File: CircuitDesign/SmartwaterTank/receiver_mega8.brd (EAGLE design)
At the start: 100 x 80 mm, 13 parts, among them IC1 MEGA8-P, T1 2N2222

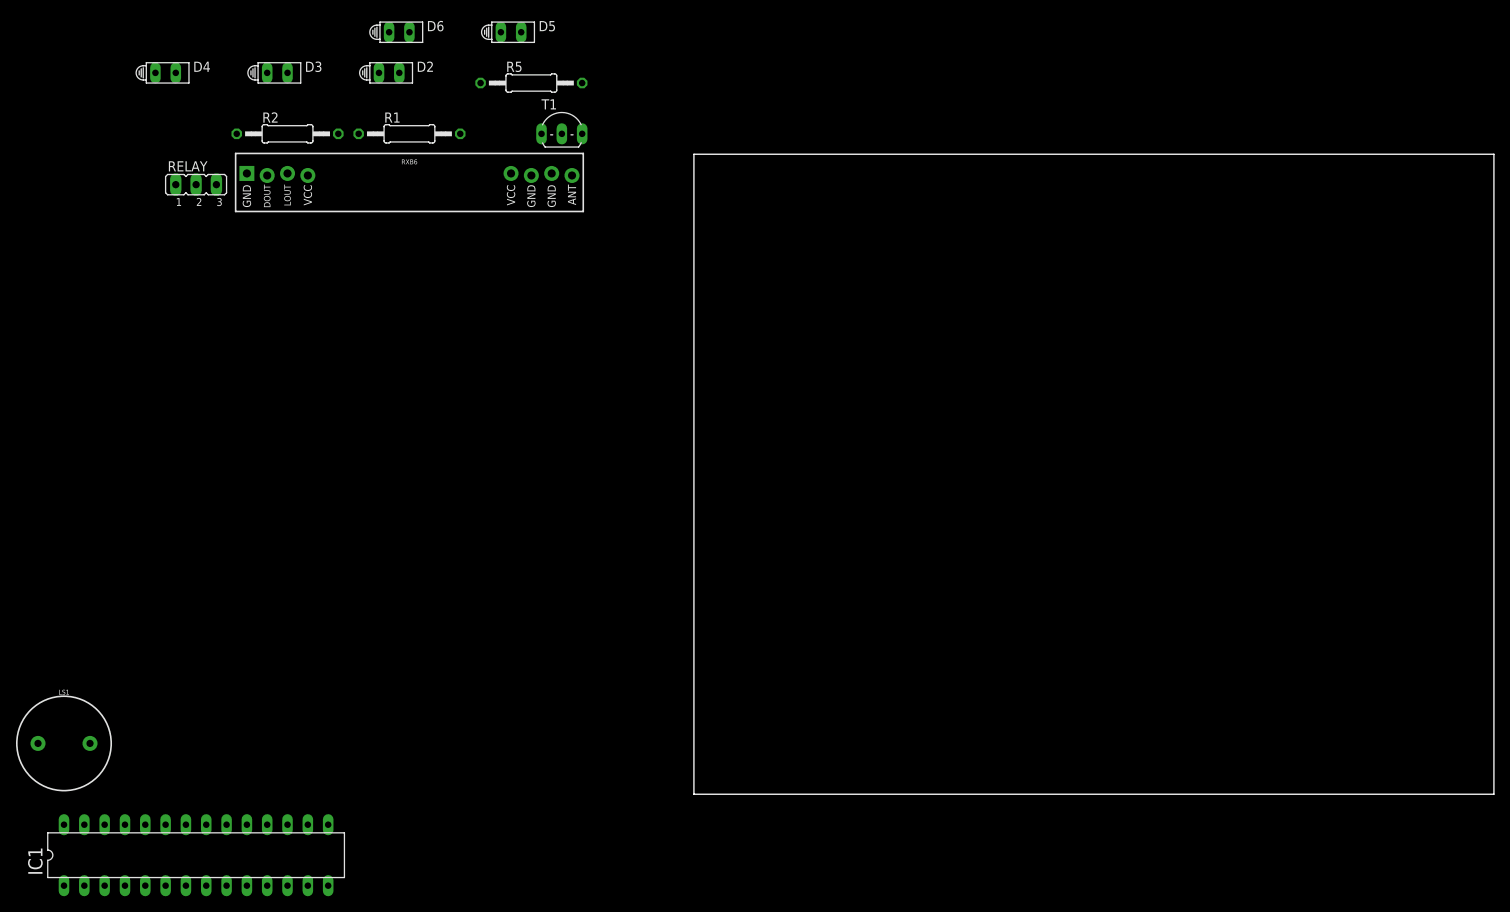
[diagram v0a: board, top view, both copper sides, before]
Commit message: Issue #6: update receiver board for vero board
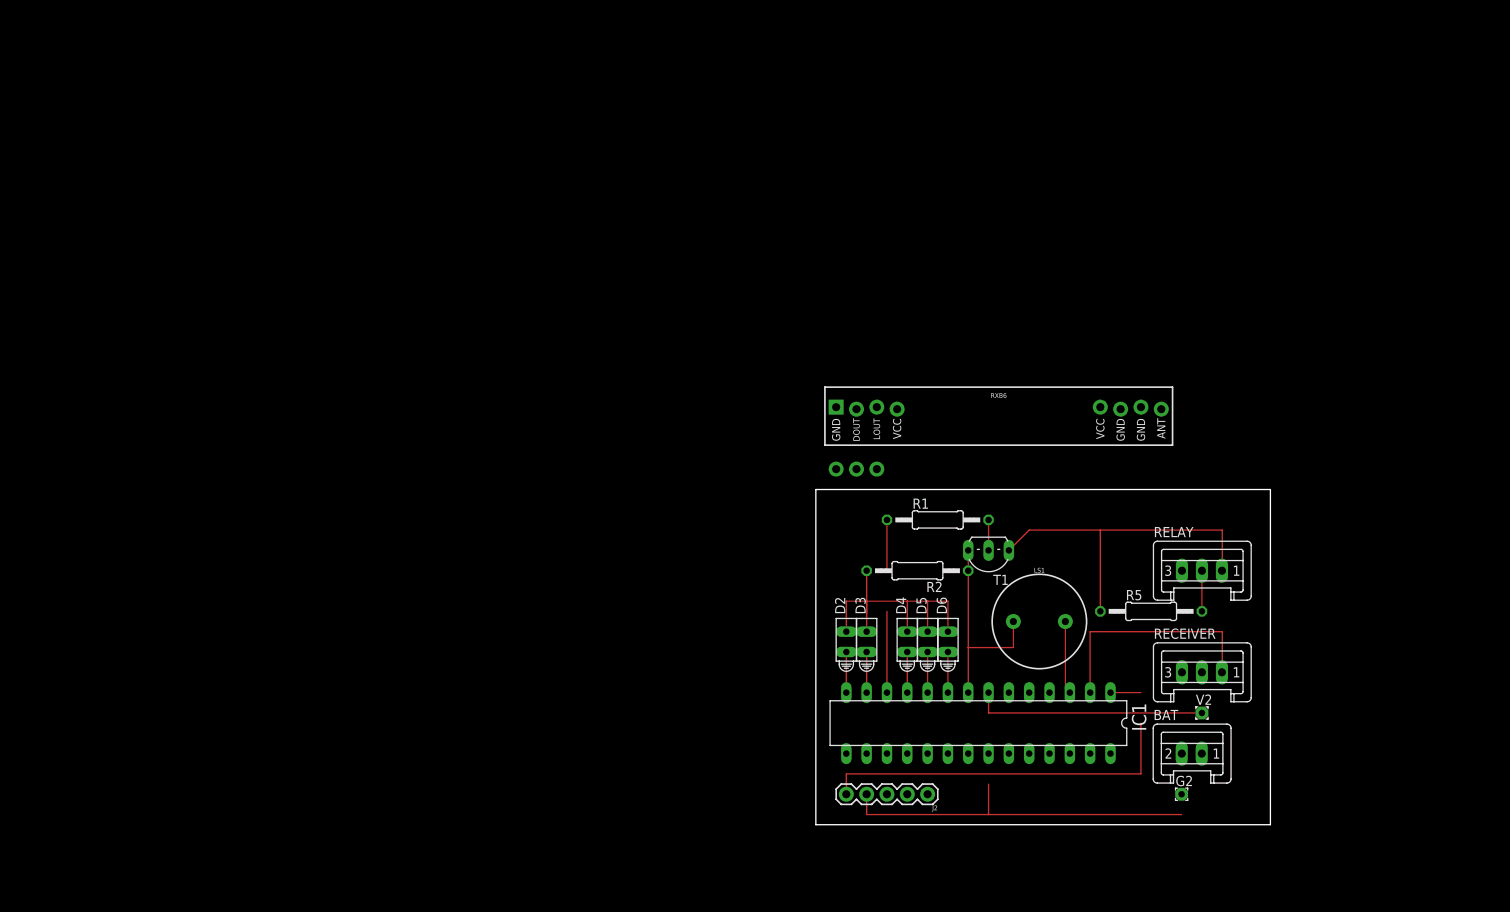
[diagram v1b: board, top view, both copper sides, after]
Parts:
- added BAT: (no value), con-amp-mt:S02P
- added G2, V2: (no value), wirepad:1,6/0,8
- added J1: (no value), SparkFun-Connectors:1X03
- added J2: (no value), SparkFun-Connectors:1X05
- added RECEIVER: (no value), con-amp-mt:S03P
- RELAY: device jumper:JP2 -> con-amp-mt:S03P
- moved RELAY 134.7 mm to (63.5, 27.9)
- moved LS1 122.9 mm to (43.2, 21.6)
- moved D4 116.8 mm to (26.7, 19.1), turned to 90 degrees
- moved D6 102.5 mm to (31.8, 19.1), turned to 90 degrees
- moved D3 102.4 mm to (21.6, 19.1), turned to 90 degrees
- moved R5 101.8 mm to (57.1, 22.9)
- moved IC1 99.2 mm to (35.6, 8.89), turned to 180 degrees
- moved R2 95.8 mm to (27.9, 27.9), turned to 180 degrees
- moved D5 92.3 mm to (29.2, 19.1), turned to 90 degrees
- moved D2 91.2 mm to (19.1, 19.1), turned to 90 degrees
- moved R1 81.8 mm to (30.5, 34.3)
- moved RXB6 79.2 mm to (38.1, 48.3)
- moved T1 74.5 mm to (36.8, 30.5), turned to 180 degrees
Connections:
- new net N$14: J1.2, RXB6.+5V@1
- new net N$16: R5.1, RELAY.1, T1.C
- new net N$17: IC1.19, J2.1
- new net N$18: IC1.18, J2.2
- new net N$19: IC1.17, J2.3
- new net N$20: IC1.15
- new net N$22: IC1.1, J2.5
- new net N$7: G2.1, IC1.22, IC1.8
- new net N$8: IC1.7, V2.1
- new net N$9: J1.3, RXB6.GND@1
- net GND: now also J2.4, RECEIVER.3; no longer IC1.22, IC1.8, RXB6.GND@1
- net N$10: now also IC1.9; no longer IC1.13
- net N$11: now also IC1.10; no longer IC1.12
- net N$13: now also IC1.13; no longer IC1.2
- net N$15: now also IC1.14; no longer IC1.27
- net N$2: now also IC1.12; no longer IC1.24
- net N$3: now also J1.1, RXB6.DATA@1; no longer R5.1, RELAY.2, T1.C
- net N$4: now also IC1.2, RECEIVER.1; no longer IC1.4, RXB6.DATA@1
- net N$5: now also IC1.3; no longer IC1.25
- net VCC: now also RECEIVER.2, RELAY.2; no longer IC1.7, RELAY.1, RXB6.+5V@1
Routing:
- net GND: track 0.00 -> 73.5 mm
- net N$22: track 0.00 -> 49.5 mm
- net N$16: track 0.00 -> 43.0 mm
- net N$6: track 0.00 -> 37.1 mm
- net N$4: track 0.00 -> 29.2 mm
- net N$8: track 0.00 -> 29.2 mm
- net N$2: track 0.00 -> 16.5 mm
- net N$5: track 0.00 -> 9.12 mm
- net VCC: track 0.00 -> 5.08 mm
- net N$15: track 0.00 -> 5.08 mm
- net N$13: track 0.00 -> 5.08 mm
- net N$12: track 0.00 -> 5.08 mm
- net N$11: track 0.00 -> 5.08 mm
- net N$10: track 0.00 -> 5.08 mm
- net N$1: track 0.00 -> 3.81 mm
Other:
- board size 100 x 80 mm -> 56.8 x 41.9 mm
